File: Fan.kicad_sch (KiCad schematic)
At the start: 5 parts, among them J18 Conn_01x02, Q6 AO3400A

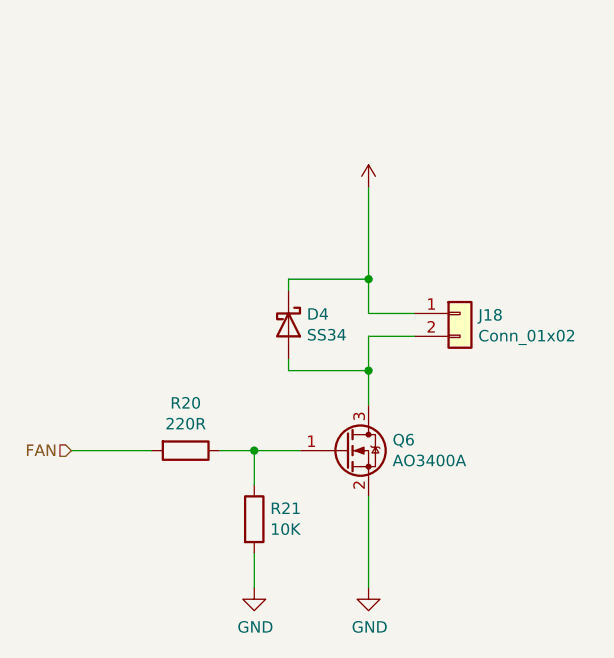
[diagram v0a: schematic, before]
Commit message: Move to KiCad v6, redesign circuit for chamber
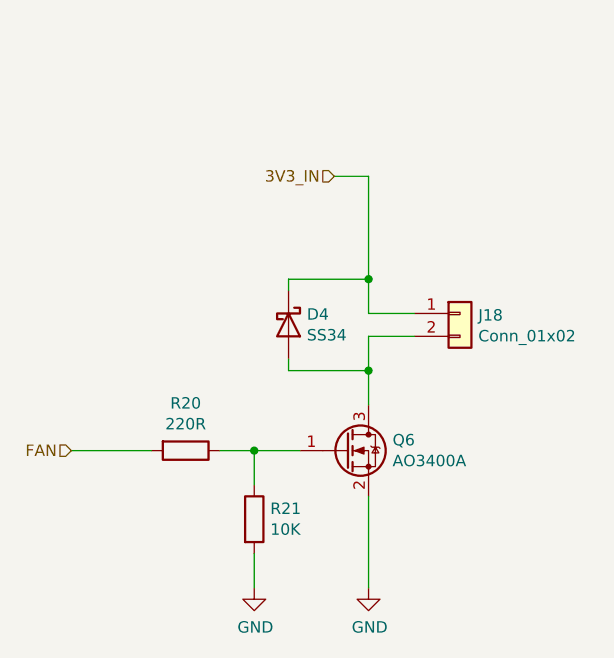
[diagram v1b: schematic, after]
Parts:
- J18: LCSC (none) -> C474881
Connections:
- net +3V3 renamed 3V3_IN
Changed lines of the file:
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@@
   (junction (at 152.4 93.98) (diameter 0) (color 0 0 0 0)
+  )
+  (wire (pts (xy 161.29 63.5) (xy 165.1 63.5))
+    (stroke (width 0) (type default) (color 0 0 0 0))
   )
   (wire (pts (xy 156.21 76.2) (xy 156.21 74.93))
@@
     (stroke (width 0) (type default) (color 0 0 0 0))
   )
-  (wire (pts (xy 165.1 64.77) (xy 165.1 74.93))
+  (wire (pts (xy 165.1 63.5) (xy 165.1 74.93))
     (stroke (width 0) (type default) (color 0 0 0 0))
   )
@@
   (wire (pts (xy 165.1 78.74) (xy 165.1 74.93))
     (stroke (width 0) (type default) (color 0 0 0 0))
+  )
+  (hierarchical_label "3V3_IN" (shape input) (at 161.29 63.5 180)
+    (effects (font (size 1.27 1.27)) (justify right))
   )
   (hierarchical_label "FAN" (shape input) (at 132.08 93.98 180)
@@
       (effects (font (size 1.27 1.27)) hide)
     )
+    (property "LCSC" "C474881" (id 4) (at 175.26 78.74 0)
+      (effects (font (size 1.27 1.27)) hide)
+    )
     (pin "1")
     (pin "2")
   )
-  (symbol (lib_id "power:+3.3V") (at 165.1 64.77 0) (unit 1)
-    (in_bom yes) (on_board yes) (fields_autoplaced)
-    (property "Reference" "#PWR?" (id 0) (at 165.1 68.58 0)
-      (effects (font (size 1.27 1.27)) hide)
-    )
-    (property "Value" "" (id 1) (at 165.1 61.1942 0))
-    (property "Footprint" "" (id 2) (at 165.1 64.77 0)
-      (effects (font (size 1.27 1.27)) hide)
-    )
-    (property "Datasheet" "" (id 3) (at 165.1 64.77 0)
-      (effects (font (size 1.27 1.27)) hide)
-    )
-    (pin "1")
-  )
 )

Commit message: Add test points, add JLC part numbers to JST XH connectors, clean up
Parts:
- J18: footprint Connector_JST:JST_XH_B2B-XH-AM_1x02_P2.50mm_Vertical -> co2_sensor_node:KF301-5.0-2P
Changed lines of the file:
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@@
       (effects (font (size 1.27 1.27)) (justify left))
     )
-    (property "Footprint" "Connector_JST:JST_XH_B2B-XH-AM_1x02_P2.50mm_Vertical" (id 2) (at 175.26 78.74 0)
+    (property "Footprint" "co2_sensor_node:KF301-5.0-2P" (id 2) (at 175.26 78.74 0)
       (effects (font (size 1.27 1.27)) hide)
     )

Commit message: Finalize schematic
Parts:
- renumbered D4 to D3, J18 to J12, Q6 to Q4, R20 to R14, R21 to R15
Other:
- title: (none) -> CO2 Chamber - Fan Driver
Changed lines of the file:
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@@
 (kicad_sch (version 20211123) (generator eeschema)
   (paper "A4")
+  (title_block
+    (title "CO2 Chamber - Fan Driver")
+    (date "2022-05-20")
+    (rev "1")
+  )
   (junction (at 165.1 85.09) (diameter 0) (color 0 0 0 0)
   )
@@
   (symbol (lib_id "Transistor_FET:AO3400A") (at 162.56 93.98 0) (unit 1)
     (in_bom yes) (on_board yes)
-    (property "Reference" "Q6" (id 0) (at 167.767 92.8116 0)
+    (property "Reference" "Q4" (id 0) (at 167.767 92.8116 0)
       (effects (font (size 1.27 1.27)) (justify left))
     )
@@
   (symbol (lib_id "Device:R") (at 144.78 93.98 270) (unit 1)
     (in_bom yes) (on_board yes)
-    (property "Reference" "R20" (id 0) (at 144.78 88.7222 90))
+    (property "Reference" "R14" (id 0) (at 144.78 88.7222 90))
     (property "Value" "220R" (id 1) (at 144.78 91.0336 90))
     (property "Footprint" "Resistor_SMD:R_0603_1608Metric" (id 2) (at 144.78 92.202 90)
@@
   (symbol (lib_id "Device:R") (at 152.4 101.6 0) (unit 1)
     (in_bom yes) (on_board yes)
-    (property "Reference" "R21" (id 0) (at 154.178 100.4316 0)
+    (property "Reference" "R15" (id 0) (at 154.178 100.4316 0)
       (effects (font (size 1.27 1.27)) (justify left))
     )
@@
   (symbol (lib_id "power:GND") (at 152.4 109.22 0) (unit 1)
     (in_bom yes) (on_board yes)
-    (property "Reference" "#PWR04" (id 0) (at 152.4 115.57 0)
+    (property "Reference" "#PWR039" (id 0) (at 152.4 115.57 0)
       (effects (font (size 1.27 1.27)) hide)
     )
@@
   (symbol (lib_id "power:GND") (at 165.1 109.22 0) (unit 1)
     (in_bom yes) (on_board yes)
-    (property "Reference" "#PWR045" (id 0) (at 165.1 115.57 0)
+    (property "Reference" "#PWR040" (id 0) (at 165.1 115.57 0)
       (effects (font (size 1.27 1.27)) hide)
     )
@@
   (symbol (lib_id "Device:D_Schottky") (at 156.21 80.01 270) (unit 1)
     (in_bom yes) (on_board yes)
-    (property "Reference" "D4" (id 0) (at 158.242 78.8416 90)
+    (property "Reference" "D3" (id 0) (at 158.242 78.8416 90)
       (effects (font (size 1.27 1.27)) (justify left))
     )
@@
   (symbol (lib_id "Connector_Generic:Conn_01x02") (at 175.26 78.74 0) (unit 1)
     (in_bom yes) (on_board yes)
-    (property "Reference" "J18" (id 0) (at 177.292 78.9432 0)
+    (property "Reference" "J12" (id 0) (at 177.292 78.9432 0)
       (effects (font (size 1.27 1.27)) (justify left))
     )

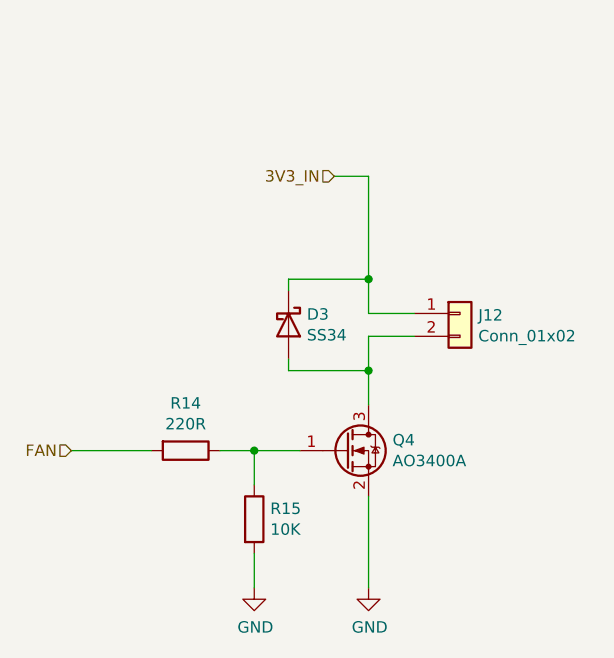
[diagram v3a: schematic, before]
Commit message: Add voltage selection header for fan
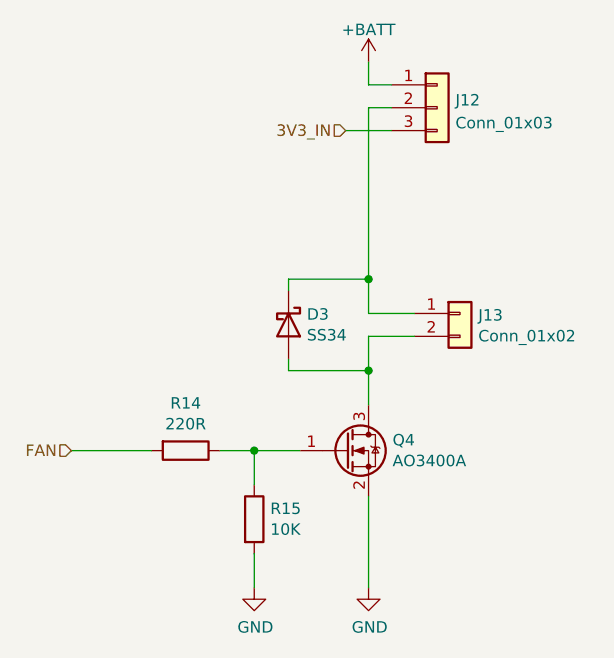
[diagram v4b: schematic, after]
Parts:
- added J12: Conn_01x03, Connector_PinHeader_2.54mm:PinHeader_1x03_P2.54mm_Vertical, symbol Connector_Generic:Conn_01x03
- renumbered J12 to J13
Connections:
- net 3V3_IN: now also J12.3 (Pin_3); no longer D3.1 (K), J13.1 (Pin_1)
- new net: D3.1 (K), J12.2 (Pin_2), J13.1 (Pin_1)
- new net +BATT: J12.1 (Pin_1)
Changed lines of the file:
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@@
   (junction (at 152.4 93.98) (diameter 0) (color 0 0 0 0)
   )
-  (wire (pts (xy 161.29 63.5) (xy 165.1 63.5))
-    (stroke (width 0) (type default) (color 0 0 0 0))
-  )
   (wire (pts (xy 156.21 76.2) (xy 156.21 74.93))
     (stroke (width 0) (type default) (color 0 0 0 0))
@@
     (stroke (width 0) (type default) (color 0 0 0 0))
   )
-  (wire (pts (xy 165.1 63.5) (xy 165.1 74.93))
+  (wire (pts (xy 165.1 55.88) (xy 165.1 74.93))
+    (stroke (width 0) (type default) (color 0 0 0 0))
+  )
+  (wire (pts (xy 165.1 53.34) (xy 165.1 50.8))
+    (stroke (width 0) (type default) (color 0 0 0 0))
+  )
+  (wire (pts (xy 165.1 55.88) (xy 167.64 55.88))
     (stroke (width 0) (type default) (color 0 0 0 0))
   )
@@
     (stroke (width 0) (type default) (color 0 0 0 0))
   )
+  (wire (pts (xy 167.64 53.34) (xy 165.1 53.34))
+    (stroke (width 0) (type default) (color 0 0 0 0))
+  )
   (wire (pts (xy 152.4 93.98) (xy 157.48 93.98))
     (stroke (width 0) (type default) (color 0 0 0 0))
@@
     (stroke (width 0) (type default) (color 0 0 0 0))
   )
+  (wire (pts (xy 162.56 58.42) (xy 167.64 58.42))
+    (stroke (width 0) (type default) (color 0 0 0 0))
+  )
   (wire (pts (xy 165.1 78.74) (xy 165.1 74.93))
     (stroke (width 0) (type default) (color 0 0 0 0))
   )
-  (hierarchical_label "3V3_IN" (shape input) (at 161.29 63.5 180)
+  (hierarchical_label "3V3_IN" (shape input) (at 162.56 58.42 180)
     (effects (font (size 1.27 1.27)) (justify right))
   )
@@
   (symbol (lib_id "power:GND") (at 165.1 109.22 0) (unit 1)
     (in_bom yes) (on_board yes)
-    (property "Reference" "#PWR040" (id 0) (at 165.1 115.57 0)
+    (property "Reference" "#PWR041" (id 0) (at 165.1 115.57 0)
       (effects (font (size 1.27 1.27)) hide)
     )
@@
   (symbol (lib_id "Connector_Generic:Conn_01x02") (at 175.26 78.74 0) (unit 1)
     (in_bom yes) (on_board yes)
-    (property "Reference" "J12" (id 0) (at 177.292 78.9432 0)
+    (property "Reference" "J13" (id 0) (at 177.292 78.9432 0)
       (effects (font (size 1.27 1.27)) (justify left))
     )
@@
     (pin "2")
   )
+  (symbol (lib_id "power:+BATT") (at 165.1 50.8 0) (unit 1)
+    (in_bom yes) (on_board yes)
+    (property "Reference" "#PWR040" (id 0) (at 165.1 54.61 0)
+      (effects (font (size 1.27 1.27)) hide)
+    )
+    (property "Value" "+BATT" (id 1) (at 165.1 47.2242 0))
+    (property "Footprint" "" (id 2) (at 165.1 50.8 0)
+      (effects (font (size 1.27 1.27)) hide)
+    )
+    (property "Datasheet" "" (id 3) (at 165.1 50.8 0)
+      (effects (font (size 1.27 1.27)) hide)
+    )
+    (pin "1")
+  )
+  (symbol (lib_id "Connector_Generic:Conn_01x03") (at 172.72 55.88 0) (unit 1)
+    (in_bom yes) (on_board yes) (fields_autoplaced)
+    (property "Reference" "J12" (id 0) (at 174.752 55.0453 0)
+      (effects (font (size 1.27 1.27)) (justify left))
+    )
+    (property "Value" "Conn_01x03" (id 1) (at 174.752 57.5822 0)
+      (effects (font (size 1.27 1.27)) (justify left))
+    )
+    (property "Footprint" "Connector_PinHeader_2.54mm:PinHeader_1x03_P2.54mm_Vertical" (id 2) (at 172.72 55.88 0)
+      (effects (font (size 1.27 1.27)) hide)
+    )
+    (property "Datasheet" "~" (id 3) (at 172.72 55.88 0)
+      (effects (font (size 1.27 1.27)) hide)
+    )
+    (property "LCSC" "C49257" (id 4) (at 172.72 55.88 0)
+      (effects (font (size 1.27 1.27)) hide)
+    )
+    (pin "1")
+    (pin "2")
+    (pin "3")
+  )
 )

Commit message: Checkpoint
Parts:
- removed J12: Conn_01x03, Connector_PinHeader_2.54mm:PinHeader_1x03_P2.54mm_Vertical, symbol Connector_Generic:Conn_01x03
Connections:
- net 3V3_IN: now also D3.1 (K), J13.1 (Pin_1)
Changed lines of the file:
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@@
     (stroke (width 0) (type default) (color 0 0 0 0))
   )
-  (wire (pts (xy 165.1 55.88) (xy 165.1 74.93))
-    (stroke (width 0) (type default) (color 0 0 0 0))
-  )
-  (wire (pts (xy 165.1 53.34) (xy 165.1 50.8))
-    (stroke (width 0) (type default) (color 0 0 0 0))
-  )
-  (wire (pts (xy 165.1 55.88) (xy 167.64 55.88))
+  (wire (pts (xy 162.56 58.42) (xy 165.1 58.42))
     (stroke (width 0) (type default) (color 0 0 0 0))
   )
   (wire (pts (xy 152.4 97.79) (xy 152.4 93.98))
+    (stroke (width 0) (type default) (color 0 0 0 0))
+  )
+  (wire (pts (xy 165.1 58.42) (xy 165.1 74.93))
     (stroke (width 0) (type default) (color 0 0 0 0))
   )
@@
   )
   (wire (pts (xy 156.21 85.09) (xy 165.1 85.09))
-    (stroke (width 0) (type default) (color 0 0 0 0))
-  )
-  (wire (pts (xy 167.64 53.34) (xy 165.1 53.34))
     (stroke (width 0) (type default) (color 0 0 0 0))
   )
@@
   )
   (wire (pts (xy 165.1 109.22) (xy 165.1 99.06))
-    (stroke (width 0) (type default) (color 0 0 0 0))
-  )
-  (wire (pts (xy 162.56 58.42) (xy 167.64 58.42))
     (stroke (width 0) (type default) (color 0 0 0 0))
   )
@@
     (pin "2")
   )
-  (symbol (lib_id "power:+BATT") (at 165.1 50.8 0) (unit 1)
-    (in_bom yes) (on_board yes)
-    (property "Reference" "#PWR040" (id 0) (at 165.1 54.61 0)
-      (effects (font (size 1.27 1.27)) hide)
-    )
-    (property "Value" "+BATT" (id 1) (at 165.1 47.2242 0))
-    (property "Footprint" "" (id 2) (at 165.1 50.8 0)
-      (effects (font (size 1.27 1.27)) hide)
-    )
-    (property "Datasheet" "" (id 3) (at 165.1 50.8 0)
-      (effects (font (size 1.27 1.27)) hide)
-    )
-    (pin "1")
-  )
-  (symbol (lib_id "Connector_Generic:Conn_01x03") (at 172.72 55.88 0) (unit 1)
-    (in_bom yes) (on_board yes) (fields_autoplaced)
-    (property "Reference" "J12" (id 0) (at 174.752 55.0453 0)
-      (effects (font (size 1.27 1.27)) (justify left))
-    )
-    (property "Value" "Conn_01x03" (id 1) (at 174.752 57.5822 0)
-      (effects (font (size 1.27 1.27)) (justify left))
-    )
-    (property "Footprint" "Connector_PinHeader_2.54mm:PinHeader_1x03_P2.54mm_Vertical" (id 2) (at 172.72 55.88 0)
-      (effects (font (size 1.27 1.27)) hide)
-    )
-    (property "Datasheet" "~" (id 3) (at 172.72 55.88 0)
-      (effects (font (size 1.27 1.27)) hide)
-    )
-    (property "LCSC" "C49257" (id 4) (at 172.72 55.88 0)
-      (effects (font (size 1.27 1.27)) hide)
-    )
-    (pin "1")
-    (pin "2")
-    (pin "3")
-  )
 )

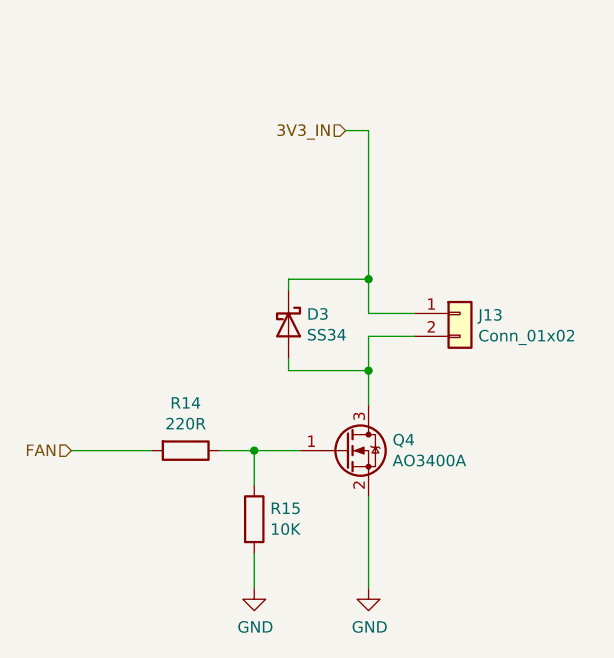
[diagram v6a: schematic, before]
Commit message: Finish rev. 2 schematic and begin PCB layout
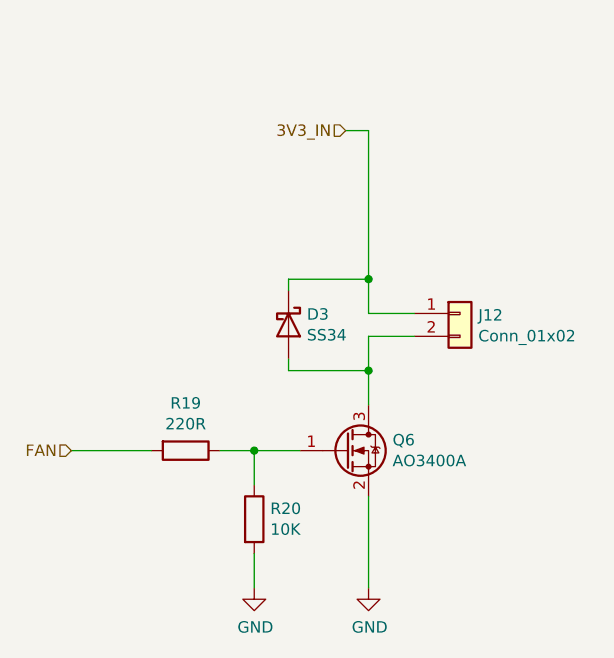
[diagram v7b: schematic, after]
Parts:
- renumbered J13 to J12, Q4 to Q6, R14 to R19, R15 to R20
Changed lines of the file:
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@@
   (symbol (lib_id "Transistor_FET:AO3400A") (at 162.56 93.98 0) (unit 1)
     (in_bom yes) (on_board yes)
-    (property "Reference" "Q4" (id 0) (at 167.767 92.8116 0)
+    (property "Reference" "Q6" (id 0) (at 167.767 92.8116 0)
       (effects (font (size 1.27 1.27)) (justify left))
     )
@@
   (symbol (lib_id "Device:R") (at 144.78 93.98 270) (unit 1)
     (in_bom yes) (on_board yes)
-    (property "Reference" "R14" (id 0) (at 144.78 88.7222 90))
+    (property "Reference" "R19" (id 0) (at 144.78 88.7222 90))
     (property "Value" "220R" (id 1) (at 144.78 91.0336 90))
     (property "Footprint" "Resistor_SMD:R_0603_1608Metric" (id 2) (at 144.78 92.202 90)
@@
   (symbol (lib_id "Device:R") (at 152.4 101.6 0) (unit 1)
     (in_bom yes) (on_board yes)
-    (property "Reference" "R15" (id 0) (at 154.178 100.4316 0)
+    (property "Reference" "R20" (id 0) (at 154.178 100.4316 0)
       (effects (font (size 1.27 1.27)) (justify left))
     )
@@
   (symbol (lib_id "power:GND") (at 152.4 109.22 0) (unit 1)
     (in_bom yes) (on_board yes)
-    (property "Reference" "#PWR039" (id 0) (at 152.4 115.57 0)
+    (property "Reference" "#PWR047" (id 0) (at 152.4 115.57 0)
       (effects (font (size 1.27 1.27)) hide)
     )
@@
   (symbol (lib_id "power:GND") (at 165.1 109.22 0) (unit 1)
     (in_bom yes) (on_board yes)
-    (property "Reference" "#PWR041" (id 0) (at 165.1 115.57 0)
+    (property "Reference" "#PWR048" (id 0) (at 165.1 115.57 0)
       (effects (font (size 1.27 1.27)) hide)
     )
@@
   (symbol (lib_id "Connector_Generic:Conn_01x02") (at 175.26 78.74 0) (unit 1)
     (in_bom yes) (on_board yes)
-    (property "Reference" "J13" (id 0) (at 177.292 78.9432 0)
+    (property "Reference" "J12" (id 0) (at 177.292 78.9432 0)
       (effects (font (size 1.27 1.27)) (justify left))
     )

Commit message: Add 5V boost converter and begin redesign of PCB
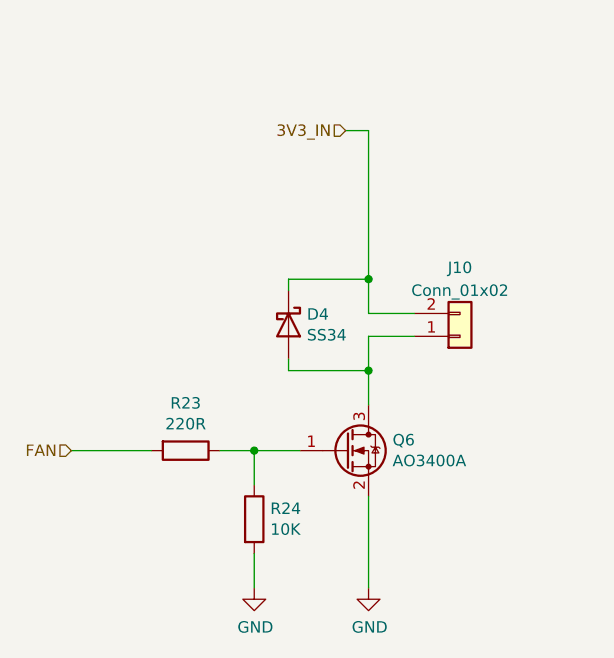
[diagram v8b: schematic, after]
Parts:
- removed J12: Conn_01x02, co2_sensor_node:KF301-5.0-2P, symbol Connector_Generic:Conn_01x02
- added J10: Conn_01x02, Connector_JST:JST_XH_B2B-XH-AM_1x02_P2.50mm_Vertical, symbol Connector_Generic:Conn_01x02
- renumbered D3 to D4, R19 to R23, R20 to R24
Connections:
- net 3V3_IN: now also J10.2 (Pin_2)
- net at D4.2 (A), Q6.3 (D): now also J10.1 (Pin_1)
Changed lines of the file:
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@@
   (symbol (lib_id "Device:R") (at 144.78 93.98 270) (unit 1)
     (in_bom yes) (on_board yes)
-    (property "Reference" "R19" (id 0) (at 144.78 88.7222 90))
+    (property "Reference" "R23" (id 0) (at 144.78 88.7222 90))
     (property "Value" "220R" (id 1) (at 144.78 91.0336 90))
     (property "Footprint" "Resistor_SMD:R_0603_1608Metric" (id 2) (at 144.78 92.202 90)
@@
   (symbol (lib_id "Device:R") (at 152.4 101.6 0) (unit 1)
     (in_bom yes) (on_board yes)
-    (property "Reference" "R20" (id 0) (at 154.178 100.4316 0)
+    (property "Reference" "R24" (id 0) (at 154.178 100.4316 0)
       (effects (font (size 1.27 1.27)) (justify left))
     )
@@
   (symbol (lib_id "power:GND") (at 152.4 109.22 0) (unit 1)
     (in_bom yes) (on_board yes)
-    (property "Reference" "#PWR047" (id 0) (at 152.4 115.57 0)
+    (property "Reference" "#PWR060" (id 0) (at 152.4 115.57 0)
       (effects (font (size 1.27 1.27)) hide)
     )
@@
   (symbol (lib_id "power:GND") (at 165.1 109.22 0) (unit 1)
     (in_bom yes) (on_board yes)
-    (property "Reference" "#PWR048" (id 0) (at 165.1 115.57 0)
+    (property "Reference" "#PWR061" (id 0) (at 165.1 115.57 0)
       (effects (font (size 1.27 1.27)) hide)
     )
@@
   (symbol (lib_id "Device:D_Schottky") (at 156.21 80.01 270) (unit 1)
     (in_bom yes) (on_board yes)
-    (property "Reference" "D3" (id 0) (at 158.242 78.8416 90)
+    (property "Reference" "D4" (id 0) (at 158.242 78.8416 90)
       (effects (font (size 1.27 1.27)) (justify left))
     )
@@
     (pin "2")
   )
-  (symbol (lib_id "Connector_Generic:Conn_01x02") (at 175.26 78.74 0) (unit 1)
+  (symbol (lib_id "Connector_Generic:Conn_01x02") (at 175.26 81.28 0) (mirror x) (unit 1)
     (in_bom yes) (on_board yes)
-    (property "Reference" "J12" (id 0) (at 177.292 78.9432 0)
-      (effects (font (size 1.27 1.27)) (justify left))
-    )
-    (property "Value" "Conn_01x02" (id 1) (at 177.292 81.2546 0)
-      (effects (font (size 1.27 1.27)) (justify left))
-    )
-    (property "Footprint" "co2_sensor_node:KF301-5.0-2P" (id 2) (at 175.26 78.74 0)
+    (property "Reference" "J10" (id 0) (at 175.26 73.66 0))
+    (property "Value" "Conn_01x02" (id 1) (at 175.26 76.2 0))
+    (property "Footprint" "Connector_JST:JST_XH_B2B-XH-AM_1x02_P2.50mm_Vertical" (id 2) (at 175.26 81.28 0)
       (effects (font (size 1.27 1.27)) hide)
     )
-    (property "Datasheet" "~" (id 3) (at 175.26 78.74 0)
+    (property "Datasheet" "~" (id 3) (at 175.26 81.28 0)
       (effects (font (size 1.27 1.27)) hide)
     )
-    (property "LCSC" "C474881" (id 4) (at 175.26 78.74 0)
+    (property "LCSC" "C20079" (id 4) (at 175.26 81.28 0)
       (effects (font (size 1.27 1.27)) hide)
     )
